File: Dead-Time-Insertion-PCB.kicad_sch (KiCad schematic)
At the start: 16 parts, among them J1 Conn_01x08_Male, Q1 MMBT3904, Q2 MMBT3904, Q3 MMBT3904, Q4 MMBT3904, Q5 MMBT3904, Q6 MMBT3904, Q7 MMBT3904, U1 74HC86

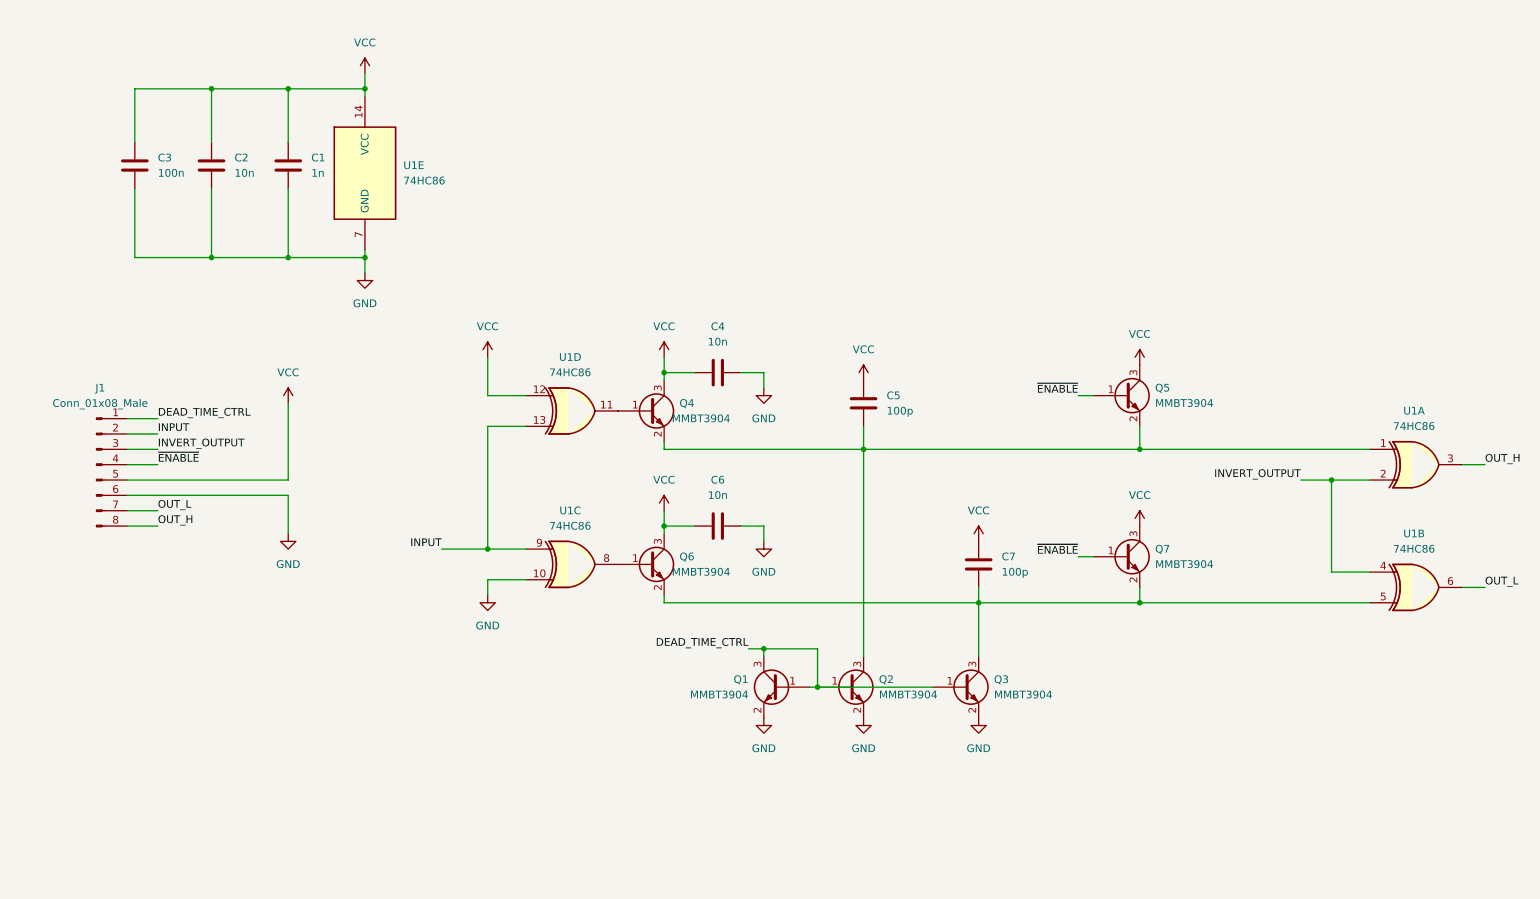
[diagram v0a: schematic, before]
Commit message: added voltage regulator so I don't blow this board up with 12V
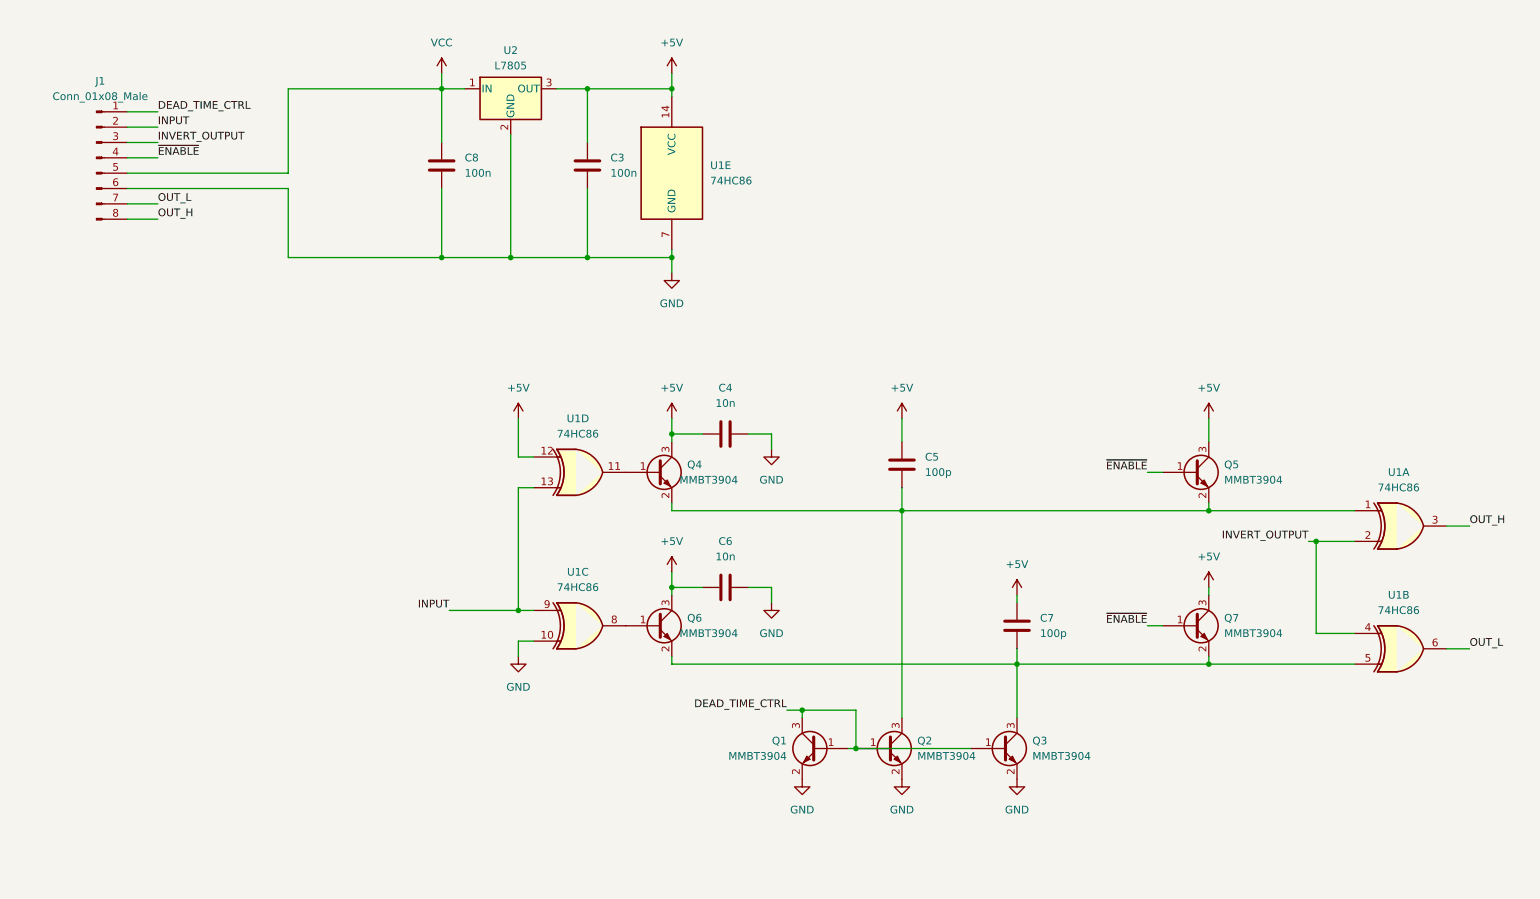
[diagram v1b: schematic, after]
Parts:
- removed C1: 1n, Capacitor_SMD:C_0603_1608Metric, symbol Device:C
- removed C2: 10n, Capacitor_SMD:C_0603_1608Metric, symbol Device:C
- added C8: 100n, Capacitor_SMD:C_0603_1608Metric, symbol Device:C
- added U2: L7805, Package_TO_SOT_SMD:SOT-89-3, symbol Regulator_Linear:L7805
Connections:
- net GND: now also C8.2, U2.2 (GND)
- net VCC: now also C8.1, U2.1 (IN); no longer C3.1, C4.1, C5.1, C6.1, C7.1, Q4.3 (C), Q5.3 (C), Q6.3 (C), Q7.3 (C), U1.12, U1.14 (VCC)
- new net +5V: C3.1, C4.1, C5.1, C6.1, C7.1, Q4.3 (C), Q5.3 (C), Q6.3 (C), Q7.3 (C), U1.12, U1.14 (VCC), U2.3 (OUT)
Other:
- moved on the sheet: C3, C4, C5, C6, C7, J1, Q1, Q2, Q3, Q4, Q5, Q6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

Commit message: addressed parasitic oscillations by adding pulldown/pullup resistors, overhauling the PCB layout to reduce the footprint of sensitive nodes, took great care to avoid cross coupling of input and output signals, added a stupid amount of vias since they are free, and improved the current sinks by replacing the package with a SOT363 transistor array to have better matching between diode-connected BJT and current sink BJT
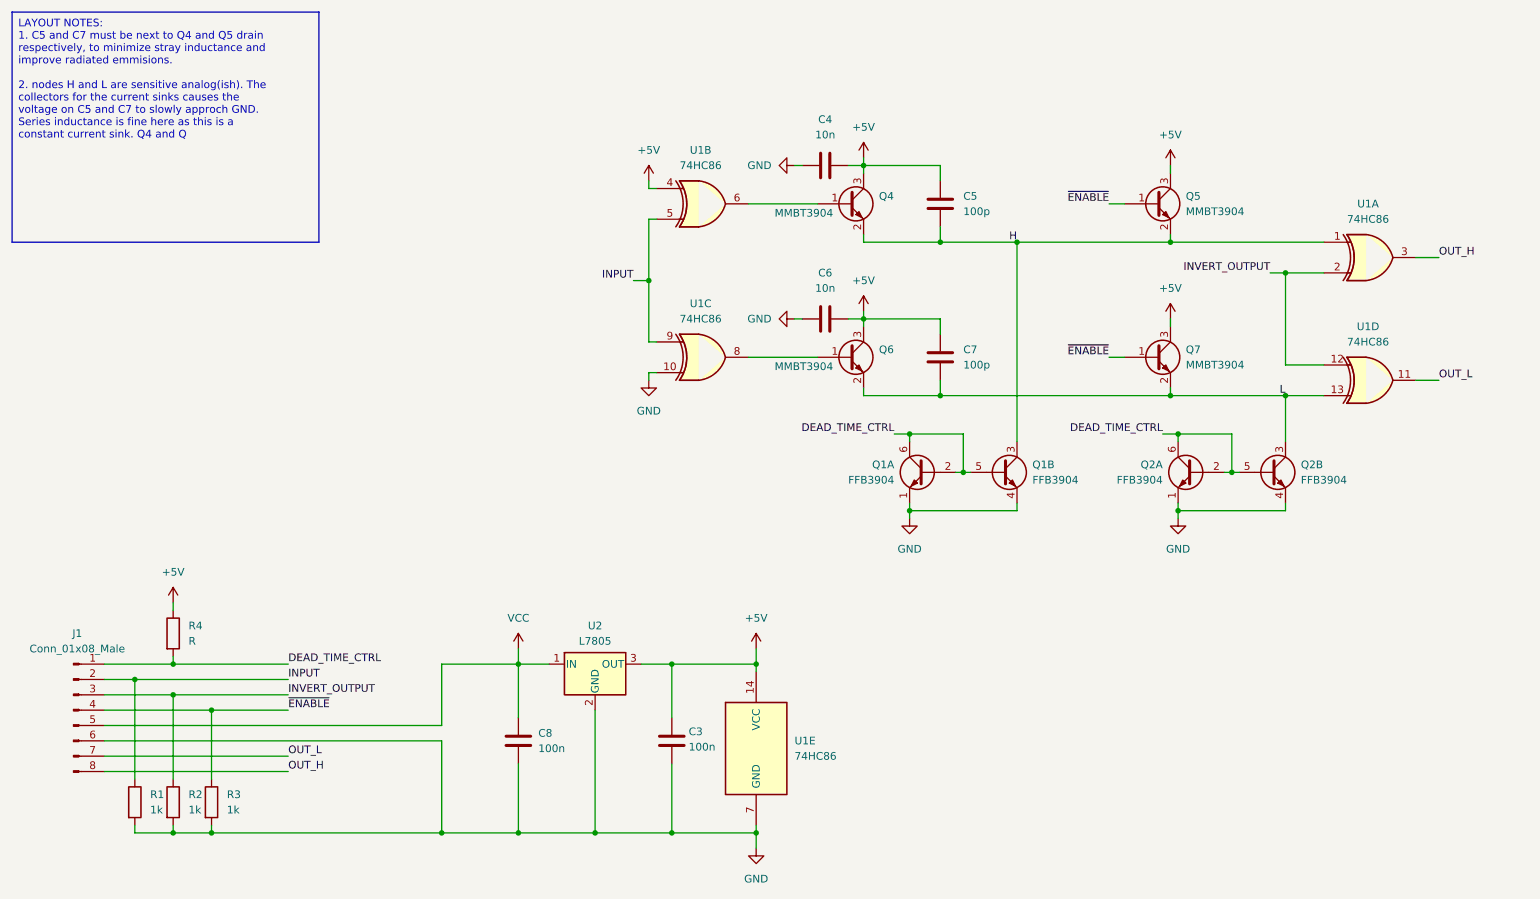
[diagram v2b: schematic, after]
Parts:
- removed Q1, Q2, Q3: MMBT3904, Package_TO_SOT_SMD:SOT-23, symbol Transistor_BJT:MMBT3904
- added Q1, Q2: FFB3904, Package_TO_SOT_SMD:SOT-363_SC-70-6, symbol Transistor_BJT:FFB3904
- added R1, R2, R3: 1k, Resistor_SMD:R_0603_1608Metric, symbol Device:R
- added R4: R, Resistor_SMD:R_0603_1608Metric, symbol Device:R
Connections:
- net +5V: now also U1.4, R4.1; no longer U1.12
- net DEAD_TIME_CTRL: now also Q1.2 (B1), Q1.5 (B2), Q1.6 (C1), Q2.2 (B1), Q2.5 (B2), Q2.6 (C1), R4.2
- net GND: now also Q1.1 (E1), Q1.4 (E2), Q2.1 (E1), Q2.4 (E2), R1.2, R2.2, R3.2
- net INPUT: now also U1.5, R1.1; no longer U1.13
- net INVERT_OUTPUT: now also U1.12, R2.1; no longer U1.4
- net OUT_L: now also U1.11; no longer U1.6
- net ~{ENABLE}: now also R3.1
- net H: now reaches C5.2, Q4.2 (E), Q5.2 (E), U1.1
- net H: now also Q1.3 (C2)
- net L: now reaches C7.2, Q6.2 (E), Q7.2 (E)
- net L: now also U1.13, Q2.3 (C2); no longer U1.5
- net at Q4.1 (B): now also U1.6; no longer U1.11
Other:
- moved on the sheet: C3, C4, C5, C6, C7, C8, J1, Q4, Q5, Q6, Q7, U1A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
